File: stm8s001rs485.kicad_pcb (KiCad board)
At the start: 2 copper layers, 33.3 x 6.3 mm, 20 parts, among them J1 Conn_02x02_Odd_Even, J2 Conn_02x03_Counter_Clockwise, U1 DS1621S, U2 STM8S001J3M, U3 XC6206P332MR, U4 SP3485CN

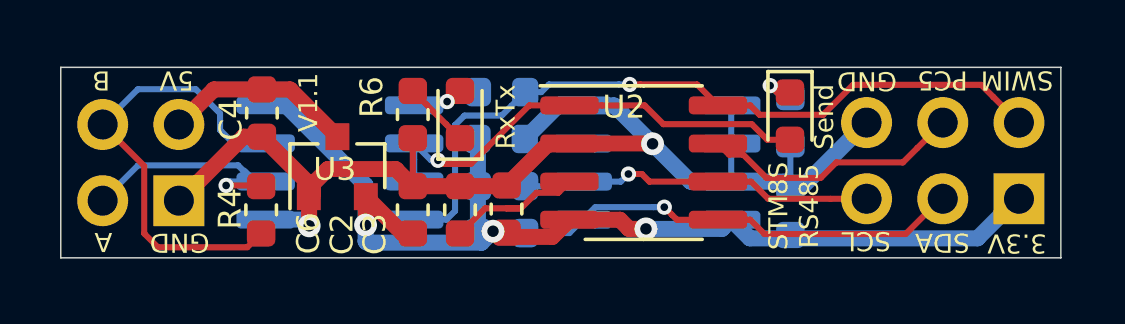
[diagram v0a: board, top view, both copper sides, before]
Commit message: V1.1 improved component placement
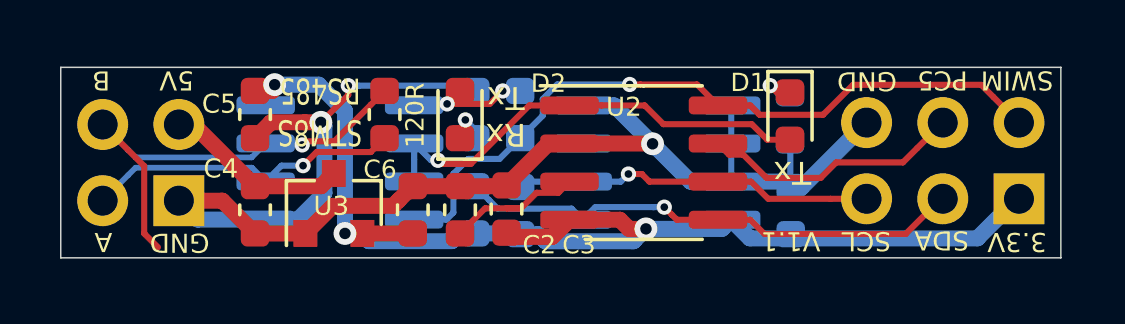
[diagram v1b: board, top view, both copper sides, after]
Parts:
- removed R4: 120R, Resistor_SMD:R_0603_1608Metric
- removed RxTx: LED green, LED_SMD:LED_0603_1608Metric
- added 120R: 120R, Resistor_SMD:R_0603_1608Metric, F.Cu at (156.0, 84.8)
- added D2: LED green, LED_SMD:LED_0603_1608Metric, F.Cu at (158.5, 84.8)
- C5: moved to F.Cu
- R6: moved to B.Cu
- moved C5 18.1 mm to (151.6, 84.8), turned to 90 degrees
- moved C1 9.94 mm to (169.5, 88.0), turned to 270 degrees
- moved C4 3.23 mm to (151.6, 87.9)
- moved R6 2.08 mm to (159.0, 84.8), turned to 90 degrees
- moved U3 1.23 mm to (154.3, 87.7)
- moved R1 1.17 mm to (159.0, 87.9), turned to 90 degrees
- moved R2 1.02 mm to (160.5, 88.0), turned to 90 degrees
- moved R3 0.97 mm to (160.5, 84.8), turned to 90 degrees
- moved R5 0.13 mm to (169.5, 84.8)
- renumbered Send to D1
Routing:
- net GND: track 43.1 -> 50.9 mm, vias 2 -> 3
- net +3V3: track 36.6 -> 40.7 mm
- net /SDA: track 15.1 -> 17.0 mm
- net /A: track 8.80 -> 10.6 mm
- net Net-(D2-Pad2): track 3.06 -> 4.47 mm, vias 1 -> 2
- net Net-(D2-Pad1): track 2.23 -> 1.43 mm, vias 0 -> 1
- net /SWIM.TX: track 25.1 -> 24.5 mm
- net /B: track 15.5 -> 15.8 mm, vias 0 -> 1
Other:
- net class Default: clearance 0.2032 -> 0.1524
- net class Power: clearance 0.2032 -> 0.1524
- rule trace_clearance: 0.2032 -> 0.1524
- board text added: "Rx Tx"
- board text added: "Tx"

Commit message: improved RX/TX LED
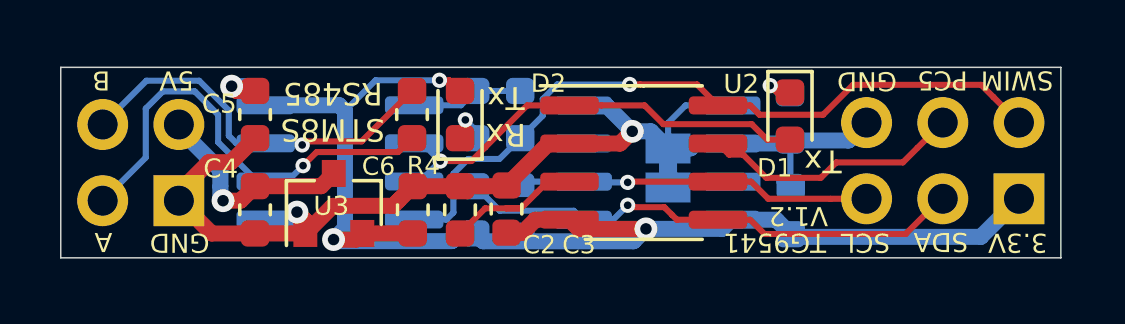
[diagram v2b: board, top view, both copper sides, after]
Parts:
- added JP1: A0, Jumper:SolderJumper-2_P1.3mm_Bridged_Pad1.0x1.5mm, B.Cu at (165.4, 86.5)
- C2, C6: value 1µF -> 1uF
- moved R4 0.91 mm to (156.9, 84.8)
- renumbered 120R to R4
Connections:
- D2 pad 2: Net-(D2-Pad2) -> +3V3
- R3 pad 2: Net-(D2-Pad2) -> Net-(R3-Pad2)
- R6 pad 2: GND -> Net-(R3-Pad2)
- U1 pad 3: (no net) -> Net-(U1-Pad3)
- U1 pad 7: GND -> Net-(JP1-Pad2)
- U4 pad 1: Net-(D2-Pad2) -> Net-(R3-Pad2)
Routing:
- net GND: track 50.9 -> 39.7 mm, vias 3 -> 2
- net +3V3: track 40.7 -> 45.7 mm, vias 3 -> 4
- net /A: track 10.6 -> 15.2 mm
- net Net-(D2-Pad2): track 4.47 -> 0.00 mm, vias 2 -> 0
- net Net-(R3-Pad2): track 0.00 -> 3.73 mm
- net Net-(JP1-Pad2): track 0.00 -> 2.19 mm
- net /B: track 15.8 -> 13.7 mm
- net +5V: track 6.56 -> 7.60 mm, vias 0 -> 1
- net /SCL: track 12.5 -> 11.9 mm
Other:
- board text added: "TG9541"
- board text added: "V1.2"
- board text removed: "V1.1"
